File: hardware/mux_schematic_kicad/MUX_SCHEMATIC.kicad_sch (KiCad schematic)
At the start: 29 parts, among them J1 CE0, J10 CNN6, J11 CNN7, J12 CNN8, J13 Conn_01x04, J2 AIN1, J3 AIN2, J4 AIN3, J5 CNN1, J6 CNN2, J7 CNN3, J8 CNN4, J9 CNN5, SW1 RESET, U1 4051, U2 4051, U3 4051, U4 4051, U5 MCP23017_SP

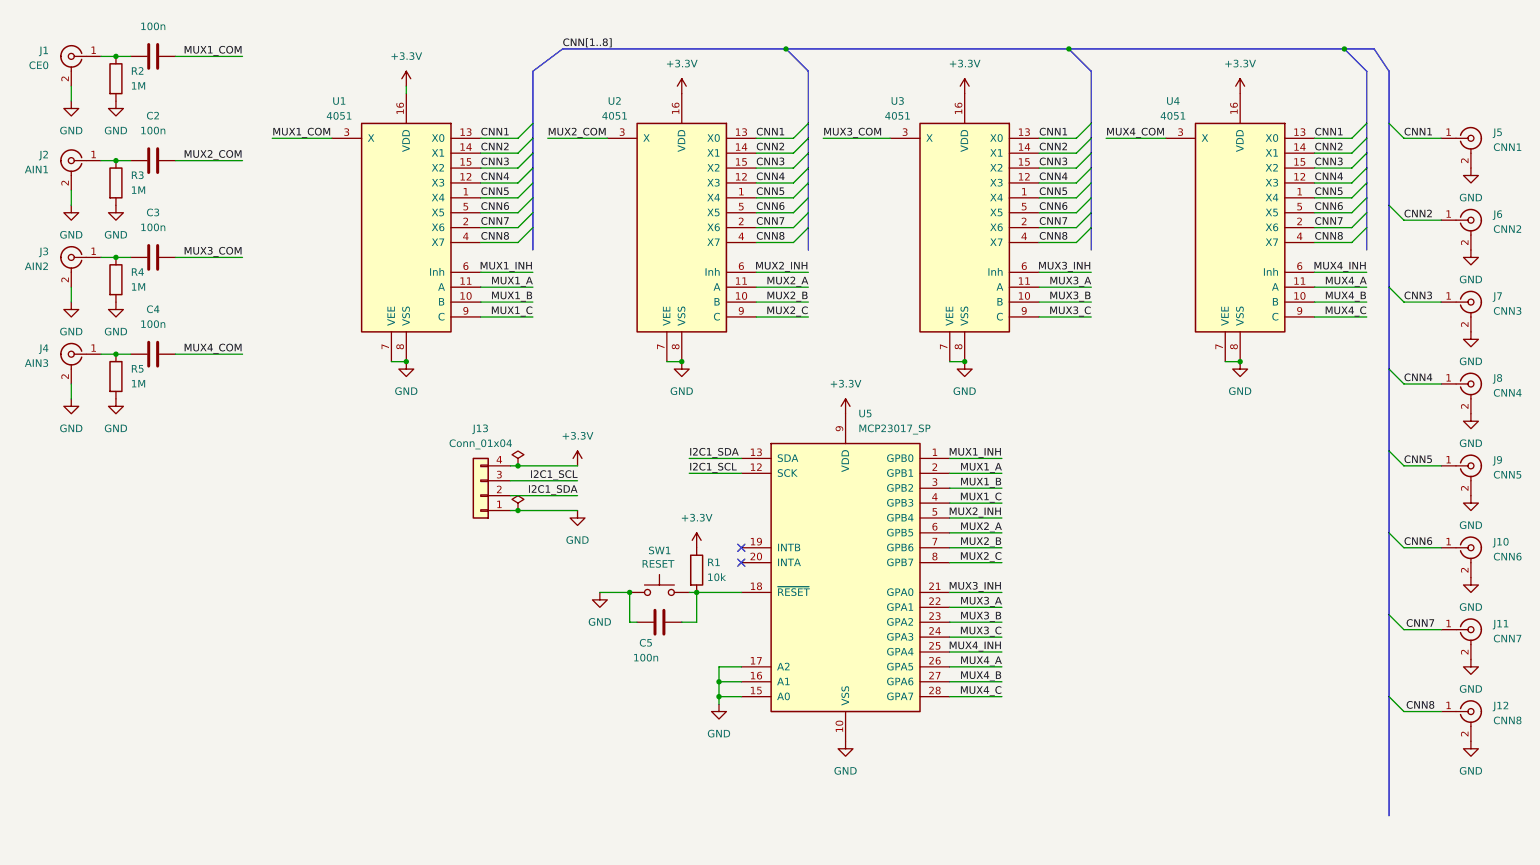
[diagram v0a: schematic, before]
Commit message: update schematic with new design (v2.0)
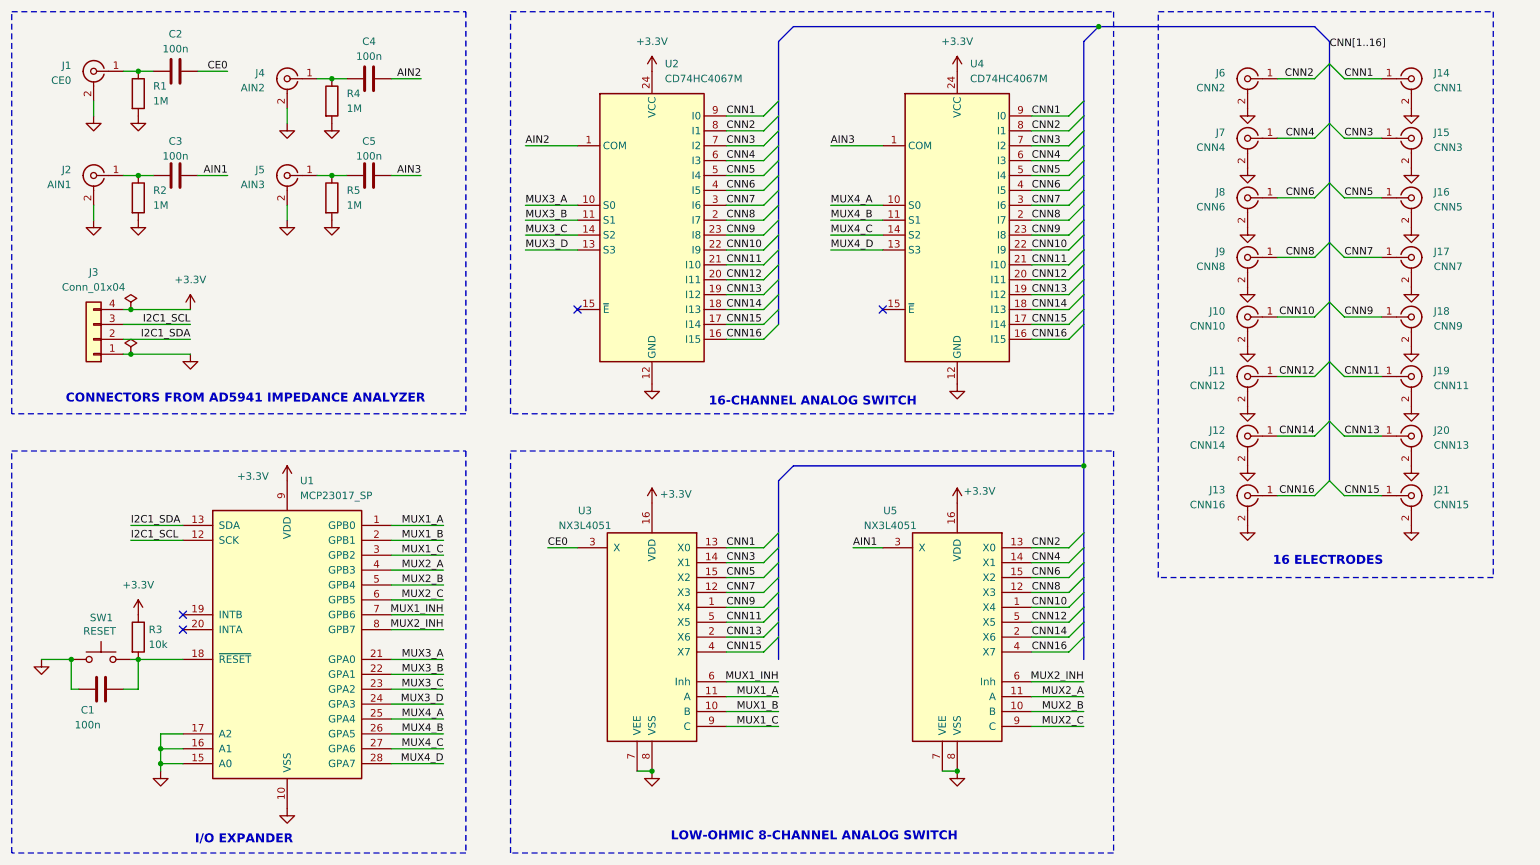
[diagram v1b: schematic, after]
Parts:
- removed U3, U4: 4051, Package_DIP:DIP-16_W7.62mm_Socket, symbol 4xxx:4051
- added J10: CNN10, Connector_PinHeader_2.54mm:PinHeader_1x02_P2.54mm_Horizontal, symbol Connector:Conn_Coaxial
- added J11: CNN12, Connector_PinHeader_2.54mm:PinHeader_1x02_P2.54mm_Horizontal, symbol Connector:Conn_Coaxial
- added J12: CNN14, Connector_PinHeader_2.54mm:PinHeader_1x02_P2.54mm_Horizontal, symbol Connector:Conn_Coaxial
- added J13: CNN16, Connector_PinHeader_2.54mm:PinHeader_1x02_P2.54mm_Horizontal, symbol Connector:Conn_Coaxial
- added J6: CNN2, Connector_PinHeader_2.54mm:PinHeader_1x02_P2.54mm_Horizontal, symbol Connector:Conn_Coaxial
- added J7: CNN4, Connector_PinHeader_2.54mm:PinHeader_1x02_P2.54mm_Horizontal, symbol Connector:Conn_Coaxial
- added J8: CNN6, Connector_PinHeader_2.54mm:PinHeader_1x02_P2.54mm_Horizontal, symbol Connector:Conn_Coaxial
- added J9: CNN8, Connector_PinHeader_2.54mm:PinHeader_1x02_P2.54mm_Horizontal, symbol Connector:Conn_Coaxial
- added U2, U4: CD74HC4067M, Package_SO:SOIC-24W_7.5x15.4mm_P1.27mm, symbol 74xx:CD74HC4067M
- J15: renamed from J6; value CNN2 -> CNN3
- J16: renamed from J7; value CNN3 -> CNN5
- J17: renamed from J8; value CNN4 -> CNN7
- J18: renamed from J9; value CNN5 -> CNN9
- J19: renamed from J10; value CNN6 -> CNN11
- J20: renamed from J11; value CNN7 -> CNN13
- J21: renamed from J12; value CNN8 -> CNN15
- U3: renamed from U1; value 4051 -> NX3L4051
- U5: renamed from U2; value 4051 -> NX3L4051
- renumbered C5 to C1, C1 to C2, C2 to C3, C3 to C4, C4 to C5, J5 to J14, J13 to J3, J3 to J4, J4 to J5, R2 to R1, R3 to R2, R1 to R3, U5 to U1
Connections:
- net MUX3_INH is gone; now on net MUX3_A: U1.21 (GPA0)
- net MUX4_INH is gone; now on net MUX4_A: U1.25 (GPA4)
- net +3.3V: now also U2.24 (VCC), U4.24 (VCC)
- net CNN1: now also U2.9 (I0), U4.9 (I0); no longer U5.13 (X0)
- net CNN2: now also U5.13 (X0), J6.1 (In), U2.8 (I1), U4.8 (I1); no longer J15.1 (In), U3.14 (X1), U5.14 (X1)
- net CNN3: now also J15.1 (In), U3.14 (X1), U2.7 (I2), U4.7 (I2); no longer J16.1 (In), U3.15 (X2), U5.15 (X2)
- net CNN4: now also U5.14 (X1), J7.1 (In), U2.6 (I3), U4.6 (I3); no longer J17.1 (In), U3.12 (X3), U5.12 (X3)
- net CNN5: now also J16.1 (In), U3.15 (X2), U2.5 (I4), U4.5 (I4); no longer J18.1 (In), U3.1 (X4), U5.1 (X4)
- net CNN6: now also U5.15 (X2), J8.1 (In), U2.4 (I5), U4.4 (I5); no longer J19.1 (In), U3.5 (X5), U5.5 (X5)
- net CNN7: now also J17.1 (In), U3.12 (X3), U2.3 (I6), U4.3 (I6); no longer J20.1 (In), U3.2 (X6), U5.2 (X6)
- net CNN8: now also U5.12 (X3), J9.1 (In), U2.2 (I7), U4.2 (I7); no longer J21.1 (In), U3.4 (X7), U5.4 (X7)
- net GND: now also J10.2 (Ext), J11.2 (Ext), J12.2 (Ext), J13.2 (Ext), J6.2 (Ext), J7.2 (Ext), J8.2 (Ext), J9.2 (Ext), U2.12 (GND), U4.12 (GND)
- net MUX1_A: now also U1.1 (GPB0); no longer U1.2 (GPB1)
- net MUX1_B: now also U1.2 (GPB1); no longer U1.3 (GPB2)
- net MUX1_C: now also U1.3 (GPB2); no longer U1.4 (GPB3)
- net MUX1_INH: now also U1.7 (GPB6); no longer U1.1 (GPB0)
- net MUX2_A: now also U1.4 (GPB3); no longer U1.6 (GPB5)
- net MUX2_B: now also U1.5 (GPB4); no longer U1.7 (GPB6)
- net MUX2_C: now also U1.6 (GPB5); no longer U1.8 (GPB7)
- net MUX2_INH: now also U1.8 (GPB7); no longer U1.5 (GPB4)
- net MUX3_A: now also U2.10 (S0); no longer U1.22 (GPA1)
- net MUX3_B: now also U1.22 (GPA1), U2.11 (S1); no longer U1.23 (GPA2)
- net MUX3_C: now also U1.23 (GPA2), U2.14 (S2); no longer U1.24 (GPA3)
- net MUX4_A: now also U4.10 (S0); no longer U1.26 (GPA5)
- net MUX4_B: now also U1.26 (GPA5), U4.11 (S1); no longer U1.27 (GPA6)
- net MUX4_C: now also U1.27 (GPA6), U4.14 (S2); no longer U1.28 (GPA7)
- net MUX1_COM renamed CE0
- net MUX2_COM renamed AIN1
- net MUX3_COM renamed AIN2
- net AIN2: now also U2.1 (COM)
- net MUX4_COM renamed AIN3
- net AIN3: now also U4.1 (COM)
- new net CNN10: J10.1 (In), U2.22 (I9), U4.22 (I9), U5.1 (X4)
- new net CNN11: J19.1 (In), U2.21 (I10), U3.5 (X5), U4.21 (I10)
- new net CNN12: J11.1 (In), U2.20 (I11), U4.20 (I11), U5.5 (X5)
- new net CNN13: J20.1 (In), U2.19 (I12), U3.2 (X6), U4.19 (I12)
- new net CNN14: J12.1 (In), U2.18 (I13), U4.18 (I13), U5.2 (X6)
- new net CNN15: J21.1 (In), U2.17 (I14), U3.4 (X7), U4.17 (I14)
- new net CNN16: J13.1 (In), U2.16 (I15), U4.16 (I15), U5.4 (X7)
- new net CNN9: J18.1 (In), U2.23 (I8), U3.1 (X4), U4.23 (I8)
- new net MUX3_D: U1.24 (GPA3), U2.13 (S3)
- new net MUX4_D: U1.28 (GPA7), U4.13 (S3)
- no-connect marks 2 -> 4
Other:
- note added: "16 ELECTRODES"
- note added: "16-CHANNEL ANALOG SWITCH"
- note added: "CONNECTORS FROM AD5941 IMPEDANCE ANALYZER"
- note added: "I/O EXPANDER"
- note added: "LOW-OHMIC 8-CHANNEL ANALOG SWITCH"
- title: (none) -> MUX circuit for AIA
- moved on the sheet: C1, C3, C4, C5, J1, J14, J15, J16, J17, J18, J19, J2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
